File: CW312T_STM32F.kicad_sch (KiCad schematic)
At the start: 21 parts, among them J1 HDR_6_2.54, P1 PCIEx4 EDGE CONNECTOR, U1 STM32F100RBT6B

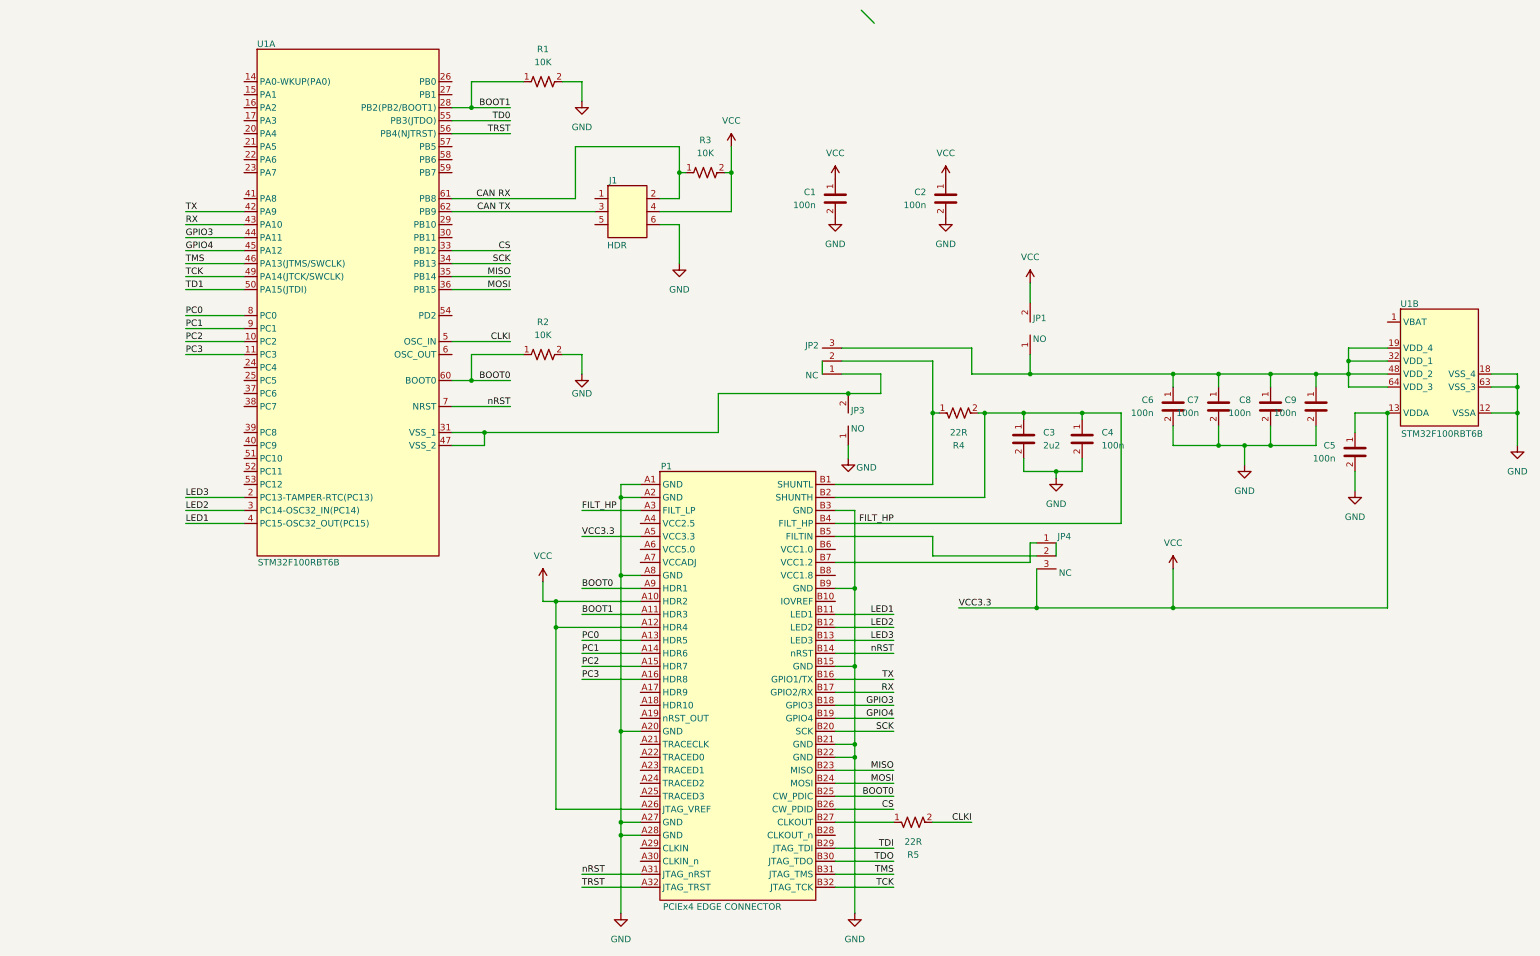
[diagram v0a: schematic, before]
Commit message: updated CW312T-STM32F1 design
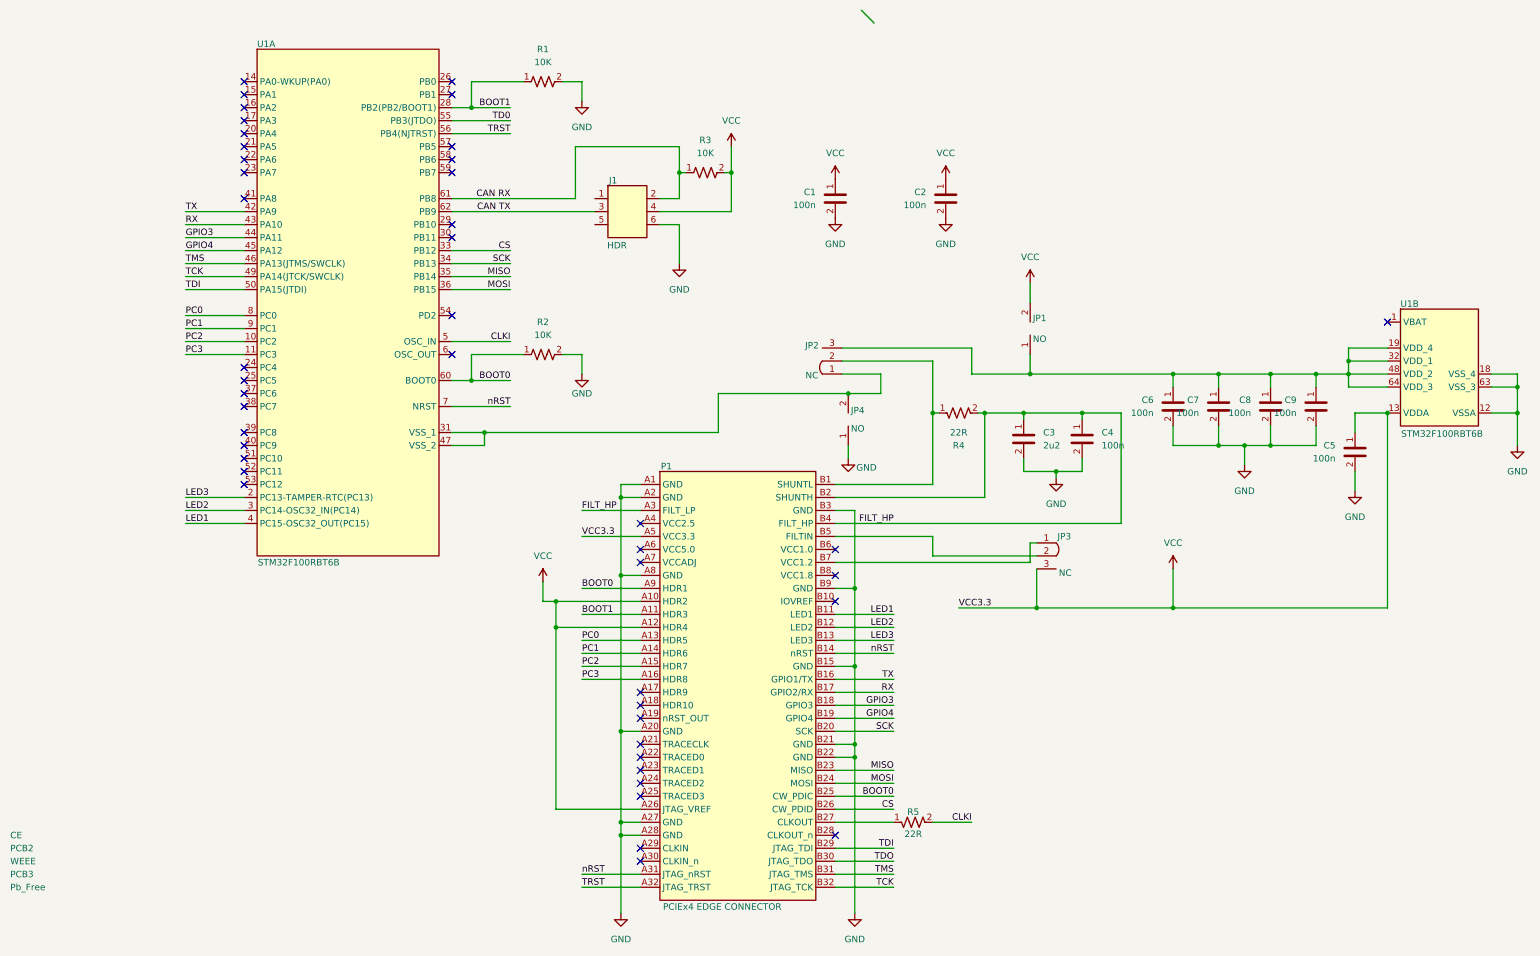
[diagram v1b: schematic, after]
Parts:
- added PCB1: CE, Silkscrren_Symbols:CE-Logo_8.5x6mm_SilkScreen, symbol Silkscreen_Symbols:CE_Free
- added PCB2: WEEE, Silkscrren_Symbols:WEEE-Logo_8.4x12mm_SilkScreen, symbol Silkscreen_Symbols:WEEE
- added PCB3: Pb_Free, Silkscrren_Symbols:Pb_Free_8.0x8.0mm_SilkScreen, symbol Silkscreen_Symbols:Pb_Free
- renumbered JP4 to JP3, JP3 to JP4
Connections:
- net TD1 is gone; now on net TDI: U1.50 (PA15(JTDI))
- no-connect marks 0 -> 45
